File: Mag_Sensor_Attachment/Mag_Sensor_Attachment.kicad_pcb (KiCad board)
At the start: 2 copper layers, 17.5 x 18.5 mm, 5 parts, among them J2 Conn_01x06_Socket, U1 MA730

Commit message: Switched connectors
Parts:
- J2: footprint Connector_Molex:Molex_Nano-Fit_105313-xx06_1x06_P2.50mm_Horizontal -> UTSVT_Connectors:Molex_MicroFit_01x06_Horizontal
- moved J2 7.76 mm to (175.8, 85.7), turned to 180 degrees
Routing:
- net /Mag_High: track 10.2 -> 14.1 mm
- net /VDD: track 8.80 -> 11.6 mm
- net /MAGSLV_Output: track 9.10 -> 11.5 mm
- net /MGSLV_Input: track 6.58 -> 8.91 mm
- net /MAG_CLK: track 12.3 -> 14.5 mm
- net /MAG_CS: track 6.82 -> 8.59 mm
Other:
- board size 17.5 x 18.5 mm -> 22.5 x 18.2 mm

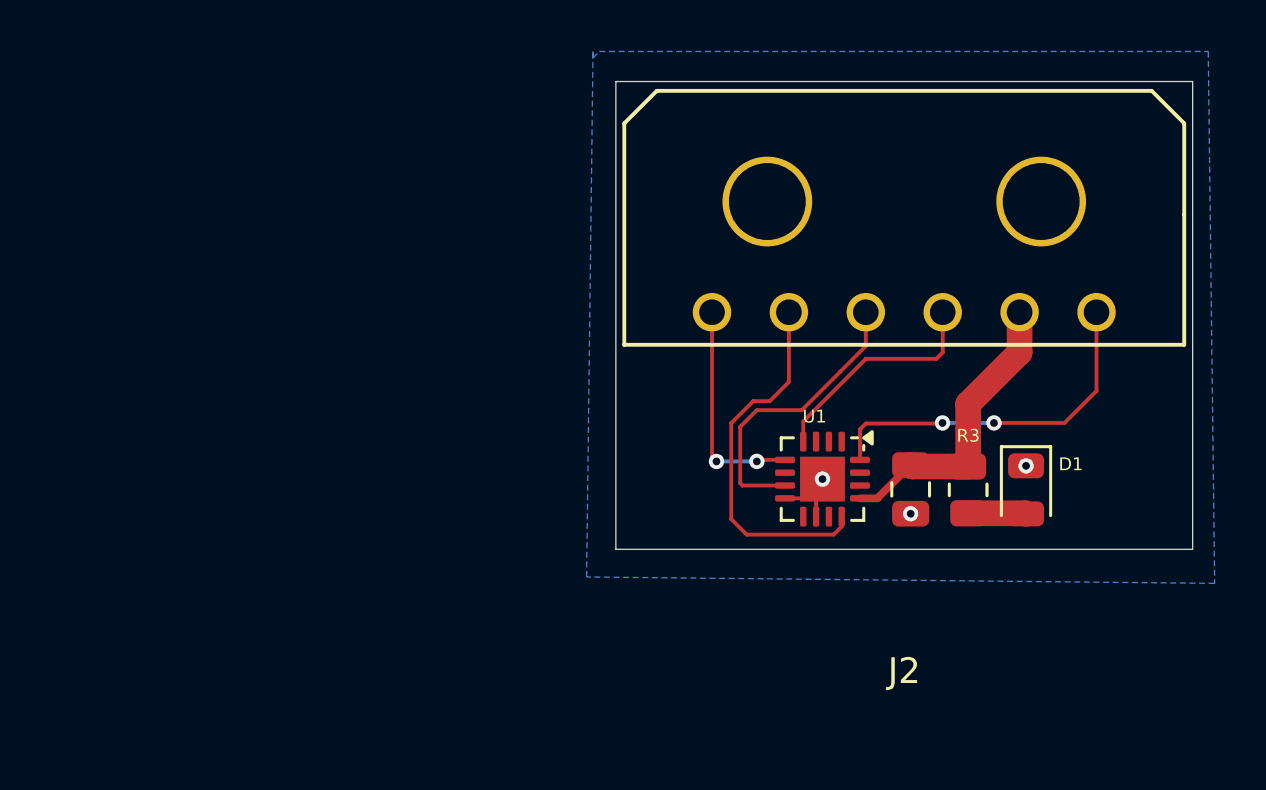
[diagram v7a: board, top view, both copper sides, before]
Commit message: Approved Connectors and gnd connected
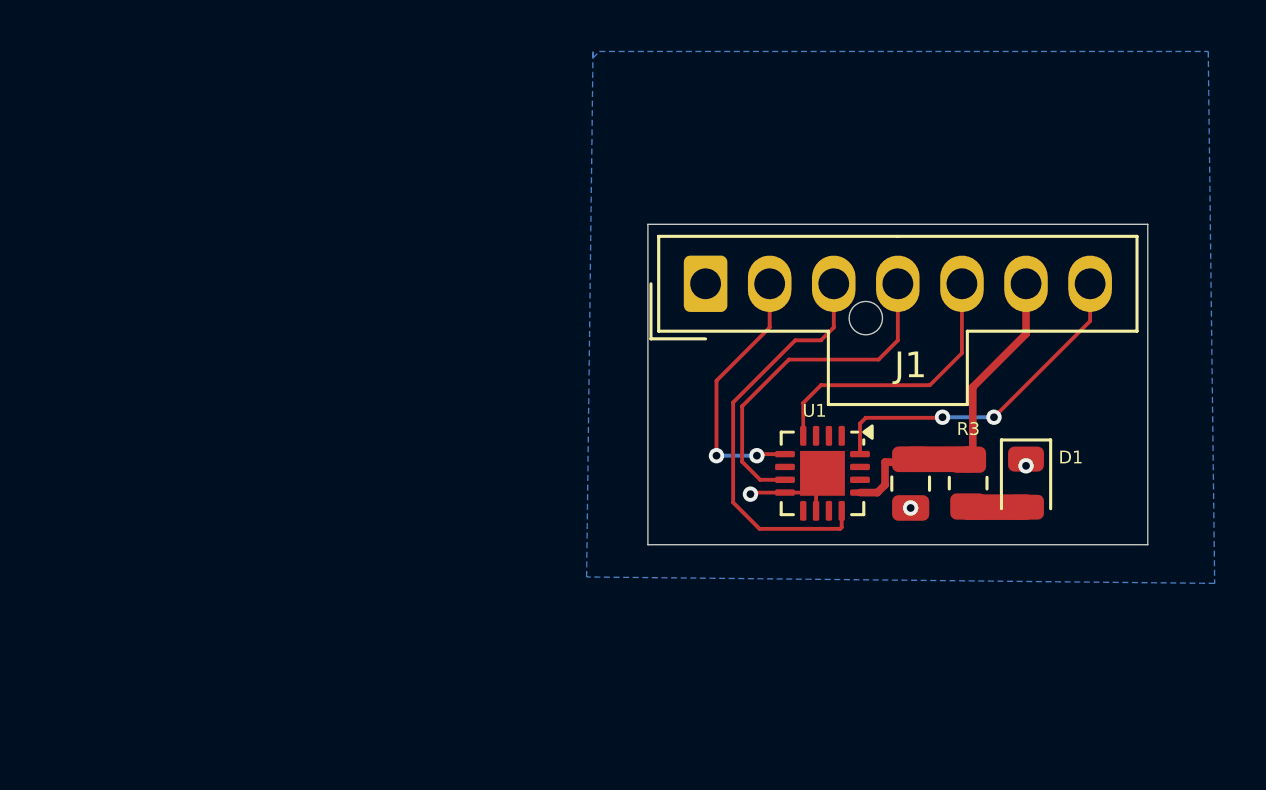
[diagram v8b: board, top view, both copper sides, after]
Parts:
- removed J2: Conn_01x06_Socket, UTSVT_Connectors:Molex_MicroFit_01x06_Horizontal
- added J1: Conn_01x07_Socket, Connector_Molex:Molex_Nano-Fit_105309-xx07_1x07_P2.50mm_Vertical, F.Cu at (168.0, 84.6)
- moved D1 0.26 mm to (180.5, 92.3)
- moved R3 0.26 mm to (178.2, 92.3)
- moved C1 0.22 mm to (176.0, 92.4)
- moved U1 0.22 mm to (172.6, 92.0)
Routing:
- net /MGSLV_Input: track 8.91 -> 11.2 mm
- net /MAGSLV_Output: track 11.5 -> 13.7 mm
- net /MAG_CS: track 8.59 -> 10.5 mm
- net /MAG_CLK: track 14.5 -> 16.3 mm
- net /VDD: track 11.6 -> 13.3 mm
- net GND: track 3.34 -> 4.71 mm
- net /Mag_High: track 14.1 -> 13.5 mm
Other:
- board size 22.5 x 18.2 mm -> 19.5 x 12.5 mm
